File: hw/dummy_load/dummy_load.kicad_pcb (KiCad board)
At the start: 4 copper layers, 100 x 87 mm, 116 parts, among them J1 12V optional, J10 Calib gain, J11 Calib divider, J12 12V in, J2 NTC DUT, J3 NTC Ambient, J4 NTC Heatsink, J5 Fan1, J6 Fan2, J7 NTC Heatsink, J8 NTC Heatsink, J9 NTC Heatsink, Q1 DMN2056U, Q10 DMG2305UX-7, Q2 IRL540NPBF, Q3 IRL540NPBF, Q4 IRL540NPBF, Q5 IRL540NPBF, Q6 IRL540NPBF, Q7 IRL540NPBF, Q8 IRL540NPBF, Q9 IRL540NPBF, U1 LM358, U2 AD620, U21 LM4040B30FTA, U3 LM4040B30FTA, U5 74HC4051, U6 AD5272BCP, U7 AD5272BCP, U8 AMS1117-5.0, X1 WAGO 2604-1102

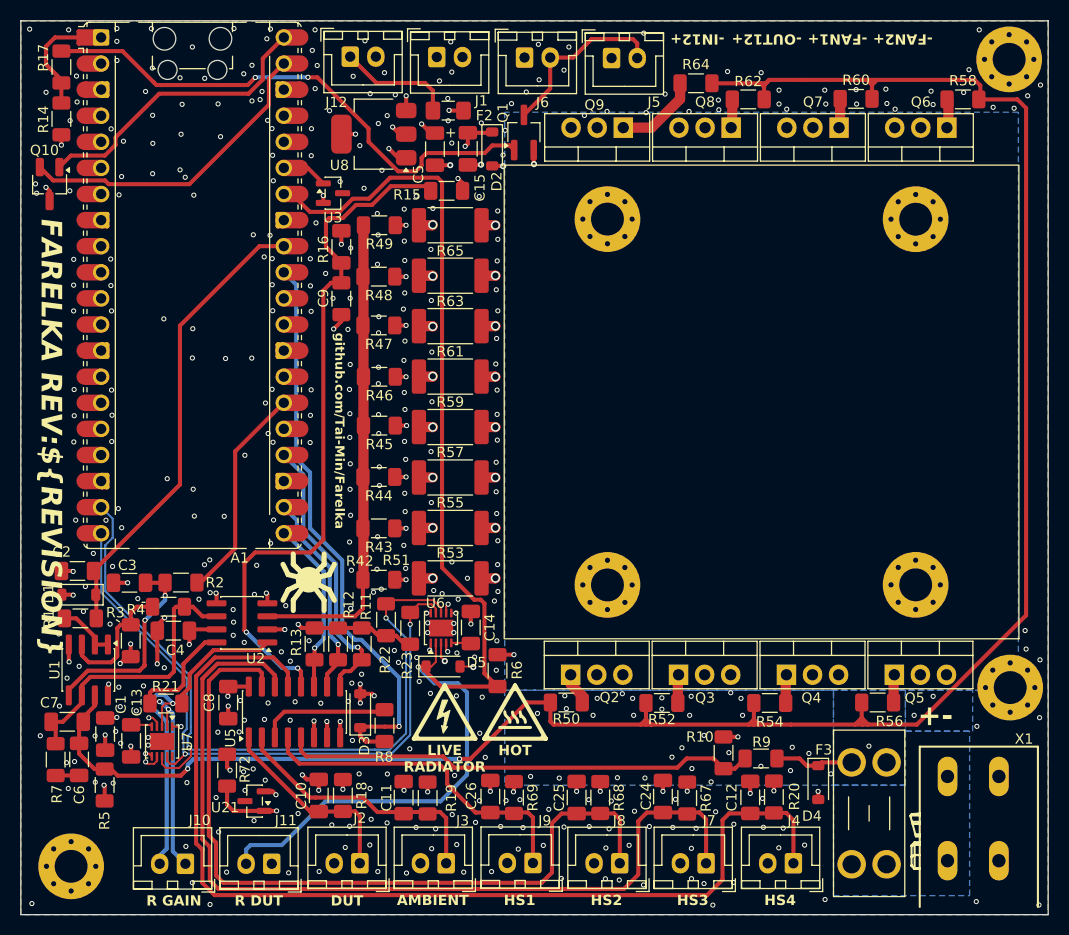
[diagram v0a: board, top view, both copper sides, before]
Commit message: Add license on silkscreen (#5)
* Add license on silkscreen

* Add more vias

---------

Signed-off-by: Mateusz Pajak <22417805+Tai-Min@users.noreply.github.com>
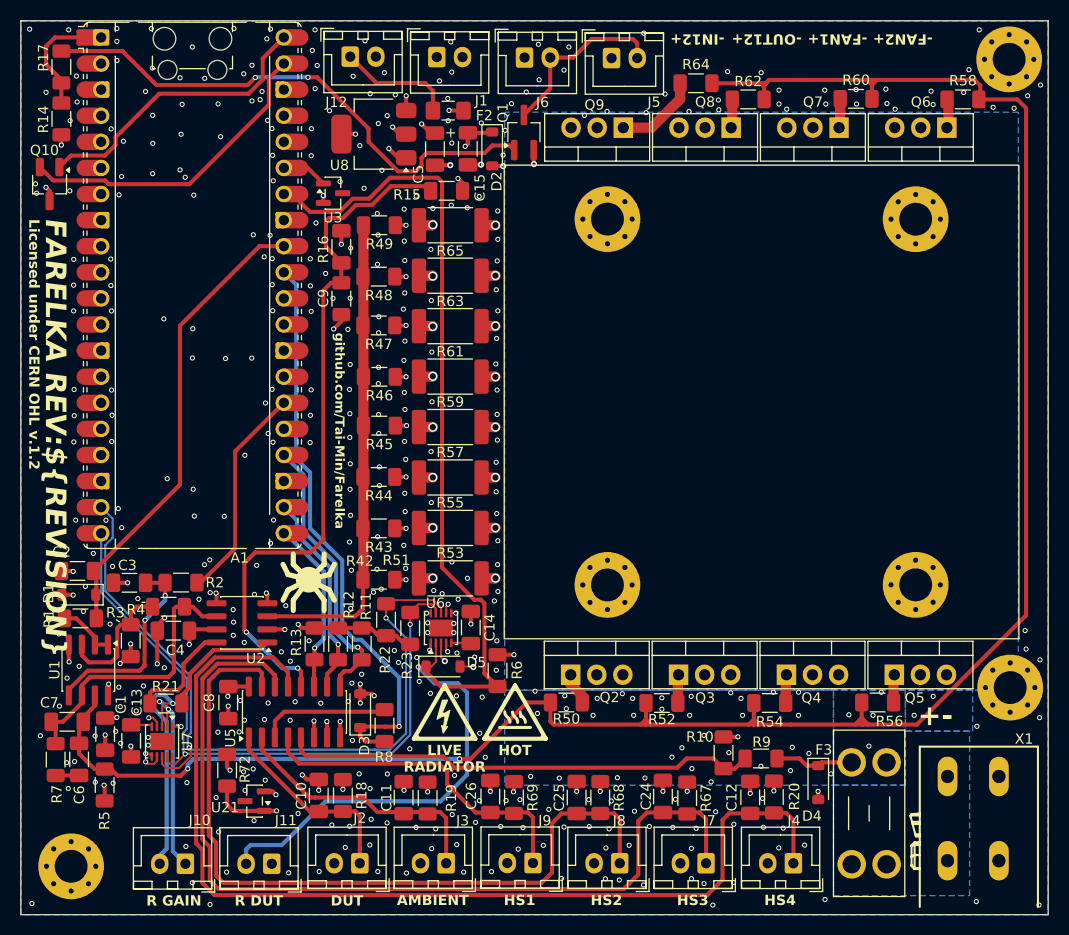
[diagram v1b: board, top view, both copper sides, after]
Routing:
- net GND: vias 466 -> 475
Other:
- board text added: "Licensed under CERN OHL v.1.2"
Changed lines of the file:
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@@
 		)
 	)
+	(gr_text "Licensed under CERN OHL v.1.2"
+		(at 100.7 75.9 270)
+		(layer "F.SilkS")
+		(effects
+			(font
+				(size 1 1)
+				(thickness 0.2)
+				(bold yes)
+			)
+			(justify bottom)
+		)
+	)
 	(gr_text "-FAN2+"
 		(at 185.85 45.6 180)
@@
 	)
 	(gr_text "FARELKA REV:${REVISION}"
-		(at 101.78 63.5 270)
+		(at 102.2 63.55 270)
 		(layer "F.SilkS" knockout)
 		(effects
@@
 	)
 	(via
+		(at 180.6 111.95)
+		(size 0.5)
+		(drill 0.3)
+		(layers "F.Cu" "B.Cu")
+		(free yes)
+		(net 4)
+	)
+	(via
 		(at 107.25 118.51)
 		(size 0.5)
@@
 	)
 	(via
+		(at 143.45 62.6)
+		(size 0.5)
+		(drill 0.3)
+		(layers "F.Cu" "B.Cu")
+		(net 4)
+	)
+	(via
 		(at 128.85 48.75)
 		(size 0.5)
@@
 	)
 	(via
+		(at 182.95 112)
+		(size 0.5)
+		(drill 0.3)
+		(layers "F.Cu" "B.Cu")
+		(free yes)
+		(net 4)
+	)
+	(via
 		(at 139.93 86.33)
 		(size 0.5)
@@
 	)
 	(via
+		(at 173.25 109.75)
+		(size 0.5)
+		(drill 0.3)
+		(layers "F.Cu" "B.Cu")
+		(free yes)
+		(net 4)
+	)
+	(via
 		(at 127.4 117.8)
 		(size 0.5)
@@
 	)
 	(via
+		(at 175.7 112)
+		(size 0.5)
+		(drill 0.3)
+		(layers "F.Cu" "B.Cu")
+		(free yes)
+		(net 4)
+	)
+	(via
 		(at 169.4 122.6)
 		(size 0.5)
@@
 	)
 	(via
+		(at 141.9 62.35)
+		(size 0.5)
+		(drill 0.3)
+		(layers "F.Cu" "B.Cu")
+		(net 4)
+	)
+	(via
 		(at 197.75 103.75)
 		(size 0.5)
@@
 	)
 	(via
+		(at 175.7 109.75)
+		(size 0.5)
+		(drill 0.3)
+		(layers "F.Cu" "B.Cu")
+		(free yes)
+		(net 4)
+	)
+	(via
 		(at 101.54 61.18)
 		(size 0.5)
@@
 	)
 	(via
+		(at 150.05 109.65)
+		(size 0.5)
+		(drill 0.3)
+		(layers "F.Cu" "B.Cu")
+		(free yes)
+		(net 4)
+	)
+	(via
 		(at 137.46 87.09)
 		(size 0.5)
@@
 	)
 	(via
+		(at 183.75 109.75)
+		(size 0.5)
+		(drill 0.3)
+		(layers "F.Cu" "B.Cu")
+		(free yes)
+		(net 4)
+	)
+	(via
 		(at 104.7 106.8)
 		(size 0.5)
@@
 	)
 	(zone
+		(net 0)
+		(net_name "")
+		(layer "F.Cu")
+		(hatch edge 0.5)
+		(connect_pads
+			(clearance 0)
+		)
+		(min_thickness 0.25)
+		(filled_areas_thickness no)
+		(keepout
+			(tracks allowed)
+			(vias allowed)
+			(pads allowed)
+			(copperpour not_allowed)
+			(footprints allowed)
+		)
+		(placement
+			(enabled no)
+			(sheetname "")
+		)
+		(fill
+			(thermal_gap 0.5)
+			(thermal_bridge_width 0.5)
+		)
+		(polygon
+			(pts
+				(xy 116.55 113.45) (xy 114.95 113.45) (xy 114.95 115.5) (xy 116.55 115.5)
+			)
+		)
+	)
+	(zone
